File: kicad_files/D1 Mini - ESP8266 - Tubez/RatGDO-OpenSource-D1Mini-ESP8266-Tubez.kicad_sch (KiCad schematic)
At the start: 20 parts, among them J1 Screw_Terminal_01x03, J2 Conn_01x11, J3 Screw_Terminal_01x02, Q1 2N7002, Q2 AO3400A, Q3 AO3400A, Q4 AO3400A, U1 WeMos_D1_mini, U2 K7805-500R3

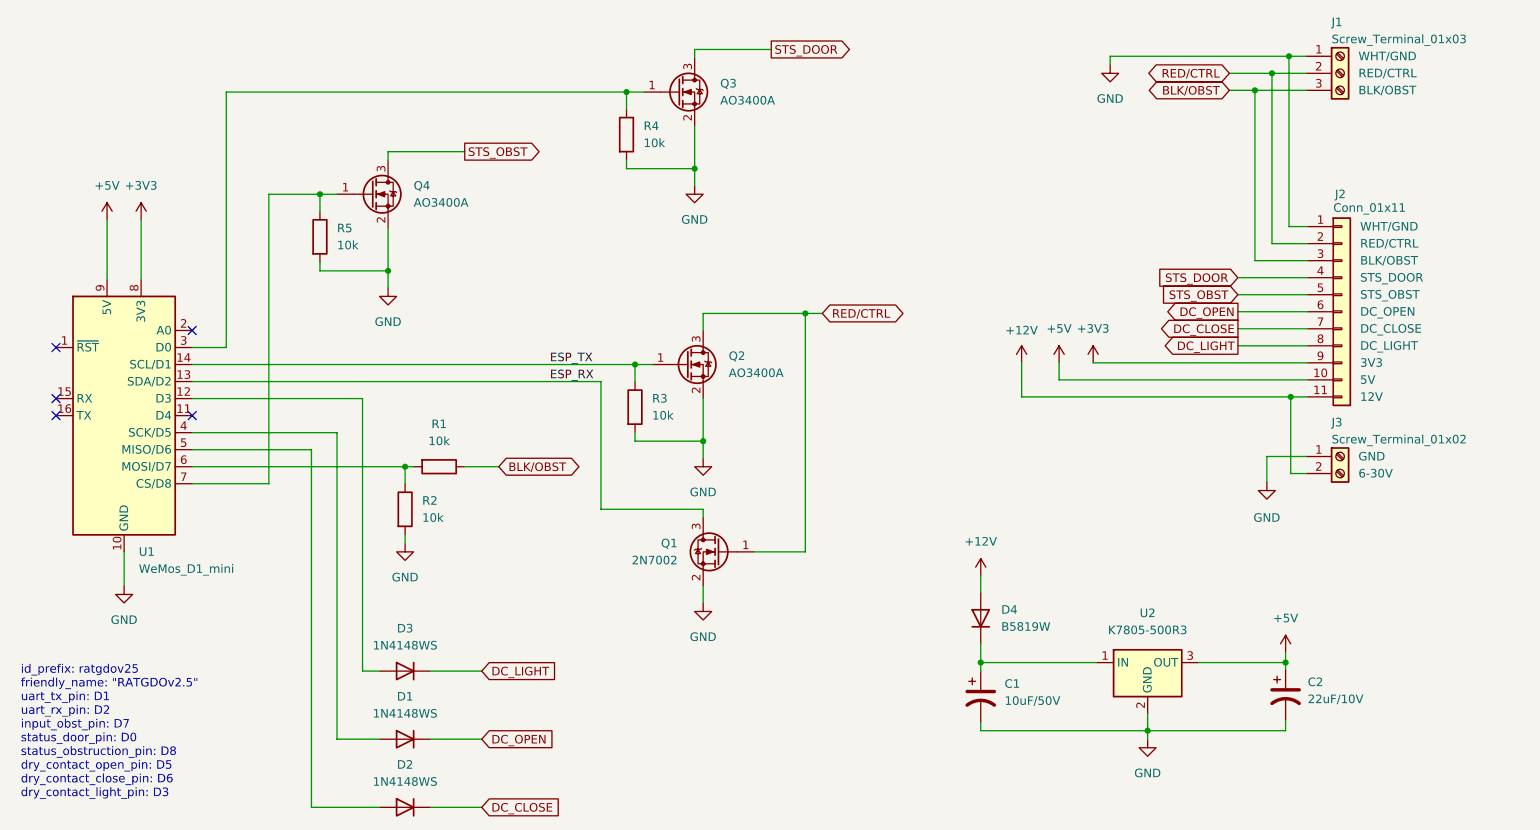
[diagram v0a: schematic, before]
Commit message: Update with potential three new v2.5 resistors.
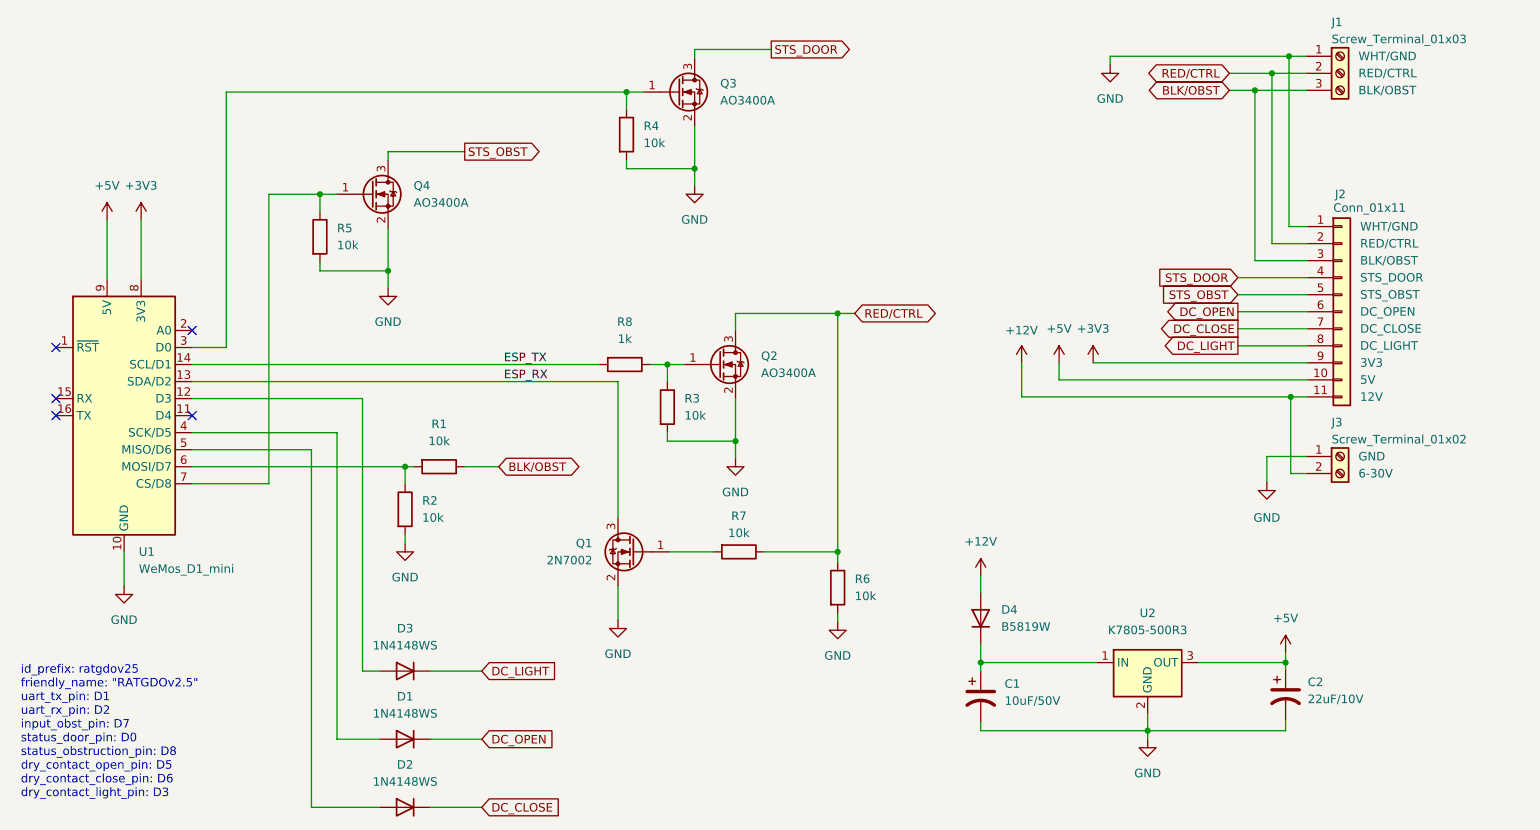
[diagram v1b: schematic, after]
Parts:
- added R6, R7: 10k, Resistor_SMD:R_0805_2012Metric_Pad1.20x1.40mm_HandSolder, symbol Device:R
- added R8: 1k, Resistor_SMD:R_0805_2012Metric_Pad1.20x1.40mm_HandSolder, symbol Device:R
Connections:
- net ESP_TX: now also R8.2; no longer Q2.1 (G), R3.1
- net GND: now also R6.2
- net RED/CTRL: now also R6.1, R7.1; no longer Q1.1 (G)
- new net: Q1.1 (G), R7.2
- new net: Q2.1 (G), R3.1, R8.1
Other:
- moved on the sheet: Q1, Q2, R3

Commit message: fix r3 connection wrt r8
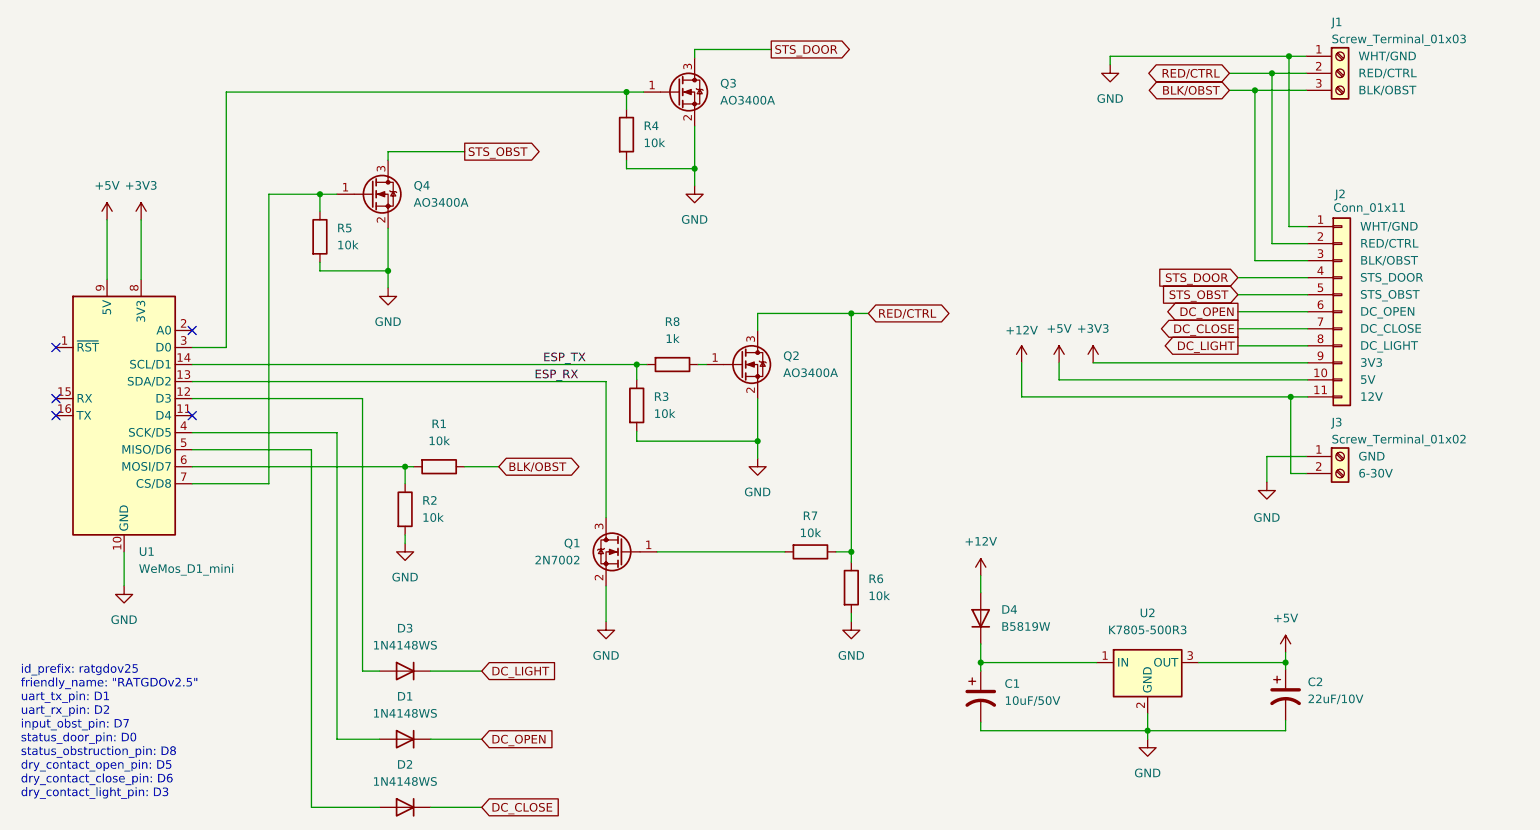
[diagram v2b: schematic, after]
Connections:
- net ESP_TX: now also R3.1
- net at Q2.1 (G), R8.1: no longer R3.1
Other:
- moved on the sheet: Q1, Q2, R3, R6, R7, R8

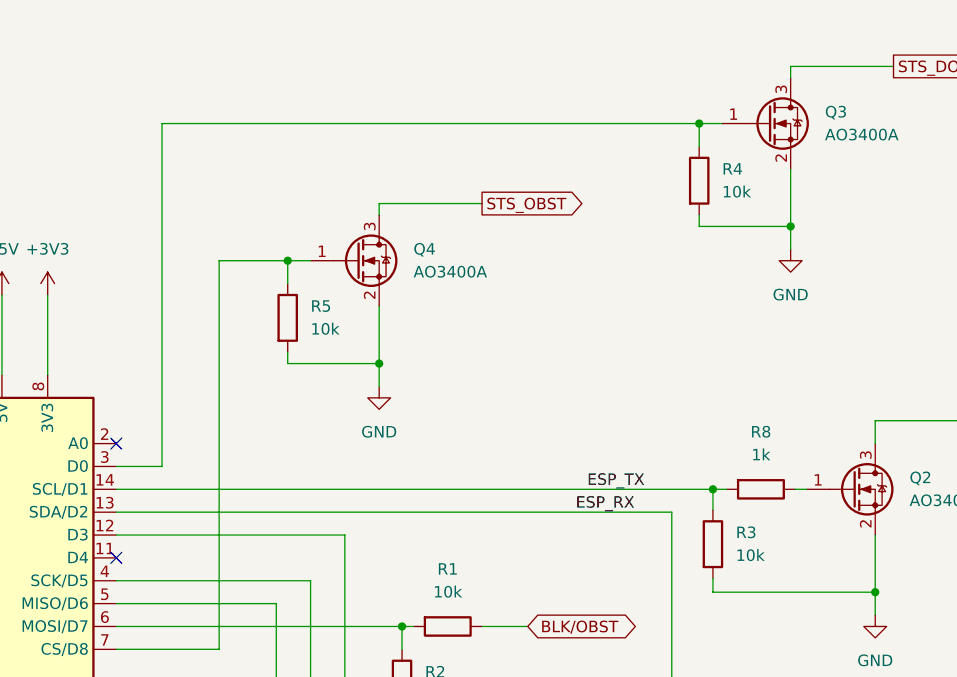
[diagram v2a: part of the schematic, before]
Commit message: Addition of R7/R6 and R8
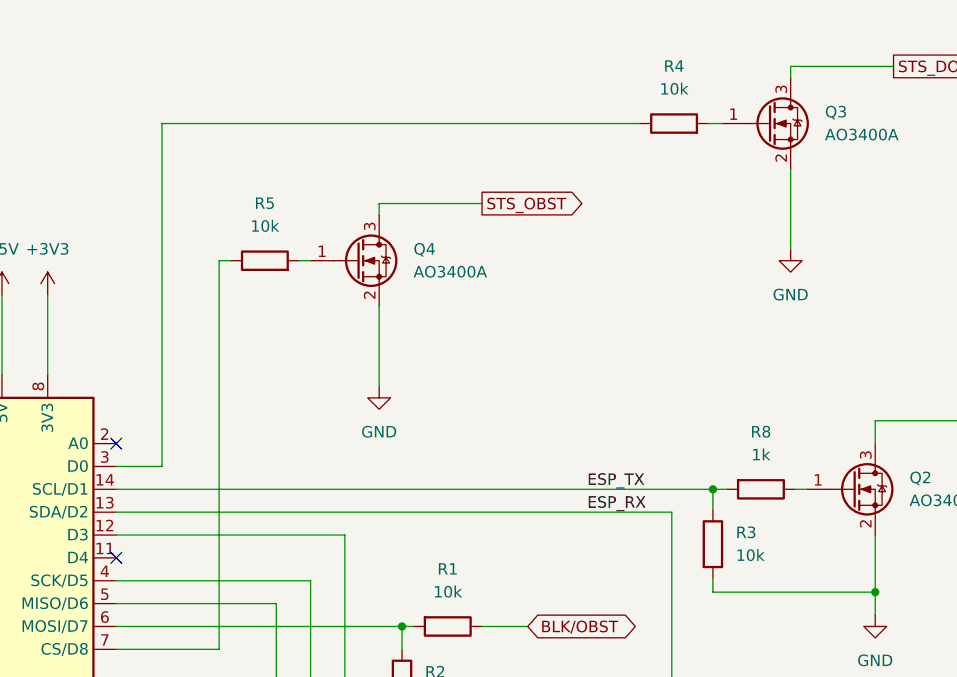
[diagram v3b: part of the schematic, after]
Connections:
- net GND: no longer R4.2, R5.2
- net at R5.1, U1.7 (CS/D8): no longer Q4.1 (G)
- net at R4.1, U1.3 (D0): no longer Q3.1 (G)
- new net: Q4.1 (G), R5.2
- new net: Q3.1 (G), R4.2
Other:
- moved on the sheet: R4, R5
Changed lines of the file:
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@@
   (junction (at 218.186 48.006) (diameter 0) (color 0 0 0 0)
   )
-  (junction (at 83.82 80.01) (diameter 0) (color 0 0 0 0)
-  )
   (junction (at 215.646 50.546) (diameter 0) (color 0 0 0 0)
   )
@@
   (junction (at 120.904 93.98) (diameter 0) (color 0 0 0 0)
   )
-  (junction (at 129.54 64.77) (diameter 0) (color 0 0 0 0)
-  )
   (junction (at 213.106 53.086) (diameter 0) (color 0 0 0 0)
-  )
-  (junction (at 73.66 68.58) (diameter 0) (color 0 0 0 0)
-  )
-  (junction (at 119.38 53.34) (diameter 0) (color 0 0 0 0)
   )
   (junction (at 218.44 98.806) (diameter 0) (color 0 0 0 0)
@@
   (no_connect (at 34.29 101.6))
   (no_connect (at 34.29 99.06))
-  (wire (pts (xy 73.66 78.74) (xy 73.66 80.01))
-    (stroke (width 0) (type default))
-  )
   (wire (pts (xy 130.048 93.98) (xy 131.318 93.98))
     (stroke (width 0) (type default))
@@
     (stroke (width 0) (type default))
   )
-  (wire (pts (xy 73.66 68.58) (xy 76.2 68.58))
-    (stroke (width 0) (type default))
-  )
   (wire (pts (xy 123.952 121.92) (xy 143.002 121.92))
     (stroke (width 0) (type default))
@@
     (stroke (width 0) (type default))
   )
-  (wire (pts (xy 59.69 53.34) (xy 119.38 53.34))
+  (wire (pts (xy 120.396 53.34) (xy 121.92 53.34))
+    (stroke (width 0) (type default))
+  )
+  (wire (pts (xy 59.69 53.34) (xy 112.776 53.34))
     (stroke (width 0) (type default))
   )
@@
     (stroke (width 0) (type default))
   )
-  (wire (pts (xy 119.38 53.34) (xy 119.38 55.88))
-    (stroke (width 0) (type default))
-  )
   (wire (pts (xy 120.904 96.266) (xy 120.904 93.98))
     (stroke (width 0) (type default))
@@
     (stroke (width 0) (type default))
   )
-  (wire (pts (xy 73.66 68.58) (xy 73.66 71.12))
-    (stroke (width 0) (type default))
-  )
   (wire (pts (xy 87.63 109.22) (xy 86.36 109.22))
     (stroke (width 0) (type default))
@@
     (stroke (width 0) (type default))
   )
-  (wire (pts (xy 119.38 64.77) (xy 129.54 64.77))
-    (stroke (width 0) (type default))
-  )
-  (wire (pts (xy 129.54 58.42) (xy 129.54 64.77))
-    (stroke (width 0) (type default))
-  )
   (wire (pts (xy 90.17 160.02) (xy 97.79 160.02))
     (stroke (width 0) (type default))
@@
     (stroke (width 0) (type default))
   )
-  (wire (pts (xy 66.04 68.58) (xy 73.66 68.58))
+  (wire (pts (xy 66.04 68.58) (xy 67.31 68.58))
     (stroke (width 0) (type default))
   )
@@
     (stroke (width 0) (type default))
   )
+  (wire (pts (xy 74.93 68.58) (xy 76.2 68.58))
+    (stroke (width 0) (type default))
+  )
   (wire (pts (xy 210.566 88.646) (xy 220.98 88.646))
     (stroke (width 0) (type default))
   )
-  (wire (pts (xy 119.38 53.34) (xy 121.92 53.34))
-    (stroke (width 0) (type default))
-  )
   (wire (pts (xy 152.908 86.36) (xy 152.908 121.92))
     (stroke (width 0) (type default))
@@
     (stroke (width 0) (type default))
   )
-  (wire (pts (xy 119.38 63.5) (xy 119.38 64.77))
-    (stroke (width 0) (type default))
-  )
   (wire (pts (xy 218.44 110.236) (xy 218.44 98.806))
     (stroke (width 0) (type default))
@@
     (stroke (width 0) (type default))
   )
-  (wire (pts (xy 73.66 80.01) (xy 83.82 80.01))
+  (wire (pts (xy 54.61 96.52) (xy 116.332 96.52))
     (stroke (width 0) (type default))
   )
@@
     (stroke (width 0) (type default))
   )
-  (wire (pts (xy 129.54 64.77) (xy 129.54 67.31))
+  (wire (pts (xy 129.54 58.42) (xy 129.54 67.31))
     (stroke (width 0) (type default))
   )
@@
     (stroke (width 0) (type default))
   )
-  (wire (pts (xy 83.82 80.01) (xy 83.82 82.55))
-    (stroke (width 0) (type default))
-  )
   (wire (pts (xy 83.82 62.23) (xy 83.82 63.5))
     (stroke (width 0) (type default))
@@
     (stroke (width 0) (type default))
   )
-  (wire (pts (xy 54.61 96.52) (xy 116.332 96.52))
-    (stroke (width 0) (type default))
-  )
   (wire (pts (xy 138.938 86.36) (xy 152.908 86.36))
     (stroke (width 0) (type default))
@@
     (stroke (width 0) (type default))
   )
-  (wire (pts (xy 83.82 73.66) (xy 83.82 80.01))
+  (wire (pts (xy 83.82 73.66) (xy 83.82 82.55))
     (stroke (width 0) (type default))
   )
@@
     (effects (font (size 1.27 1.27)) (justify left bottom))
   )
-  (label "ESP_RX" (at 105.664 96.52 0) (fields_autoplaced)
+  (label "ESP_RX" (at 106.934 96.52 0) (fields_autoplaced)
     (effects (font (size 1.27 1.27)) (justify left bottom))
   )
@@
     )
   )
-  (symbol (lib_id "Device:R") (at 73.66 74.93 0) (unit 1)
-    (in_bom yes) (on_board yes) (dnp no) (fields_autoplaced)
-    (property "Reference" "R5" (at 76.2 73.66 0)
-      (effects (font (size 1.27 1.27)) (justify left))
-    )
-    (property "Value" "10k" (at 76.2 76.2 0)
-      (effects (font (size 1.27 1.27)) (justify left))
-    )
-    (property "Footprint" "Resistor_SMD:R_0805_2012Metric_Pad1.20x1.40mm_HandSolder" (at 71.882 74.93 90)
-      (effects (font (size 1.27 1.27)) hide)
-    )
-    (property "Datasheet" "~" (at 73.66 74.93 0)
+  (symbol (lib_id "Device:R") (at 71.12 68.58 90) (unit 1)
+    (in_bom yes) (on_board yes) (dnp no) (fields_autoplaced)
+    (property "Reference" "R5" (at 71.12 62.23 90)
+      (effects (font (size 1.27 1.27)))
+    )
+    (property "Value" "10k" (at 71.12 64.77 90)
+      (effects (font (size 1.27 1.27)))
+    )
+    (property "Footprint" "Resistor_SMD:R_0805_2012Metric_Pad1.20x1.40mm_HandSolder" (at 71.12 70.358 90)
+      (effects (font (size 1.27 1.27)) hide)
+    )
+    (property "Datasheet" "~" (at 71.12 68.58 0)
       (effects (font (size 1.27 1.27)) hide)
     )
@@
     )
   )
-  (symbol (lib_id "Device:R") (at 119.38 59.69 0) (unit 1)
-    (in_bom yes) (on_board yes) (dnp no) (fields_autoplaced)
-    (property "Reference" "R4" (at 121.92 58.42 0)
-      (effects (font (size 1.27 1.27)) (justify left))
-    )
-    (property "Value" "10k" (at 121.92 60.96 0)
-      (effects (font (size 1.27 1.27)) (justify left))
-    )
-    (property "Footprint" "Resistor_SMD:R_0805_2012Metric_Pad1.20x1.40mm_HandSolder" (at 117.602 59.69 90)
-      (effects (font (size 1.27 1.27)) hide)
-    )
-    (property "Datasheet" "~" (at 119.38 59.69 0)
-      (effects (font (size 1.27 1.27)) hide)
-    )
+  (symbol (lib_id "Device:R") (at 116.586 53.34 90) (unit 1)
+    (in_bom yes) (on_board yes) (dnp no) (fields_autoplaced)
+    (property "Reference" "R4" (at 116.586 46.99 90)
+      (effects (font (size 1.27 1.27)))
+    )
+    (property "Value" "10k" (at 116.586 49.53 90)
+      (effects (font (size 1.27 1.27)))
+    )
+    (property "Footprint" "Resistor_SMD:R_0805_2012Metric_Pad1.20x1.40mm_HandSolder" (at 116.586 55.118 90)
+      (effects (font (size 1.27 1.27)) hide)
+    )
+    (property "Datasheet" "~" (at 116.586 53.34 0)
+      (effects (font (size 1.27 1.27)) hide)
+    )
